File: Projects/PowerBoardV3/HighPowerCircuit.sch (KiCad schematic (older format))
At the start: 0 parts

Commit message: Added High Power Schematic
Added power Transistors
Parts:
- added D?: D_Small_ALT, symbol D_Small_ALT
- added J?: BATT, symbol Conn_01x02
- added Q? (x2): IRF3205, TO_SOT_Packages_THT:TO-220_Vertical, symbol IRF3205
- added Q?: BSS84, TO_SOT_Packages_SMD:SOT-23, symbol BSS84
- added R? (x2): 1M, symbol R_Small
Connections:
- new net: D?.1 (K), Q?.1 (G), R?.1, R?.2
- new net: D?.2 (A), Q?.3 (D), R?.1
- new net BATT+: J?.2 (Pin_2)
- new net BATT-: J?.1 (Pin_1), Q?.3 (S), R?.2
- new net CHG: Q?.2 (S)
- new net CHG_T: Q?.2 (D), Q?.2 (D)
- new net DSH: Q?.1 (G)
- new net GND: Q?.1 (G)
- new net SENSE_R: Q?.3 (S)
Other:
- note added: "High Power Circuit with Connectors\n"

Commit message: Changes to High Power Circuit
Added a bunch of changes that can be seen on the change log
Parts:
- added C? (x18): 680uF, symbol CP
- added J?: M3-ATX-20-PWR, symbol Conn_01x02
- added J?: Cell Voltage Sense, symbol Conn_02x04_Counter_Clockwise
- added J?: MC_STACK_1, symbol Conn_01x06
- added J?: MC_STACK_2, symbol Conn_01x06
- added J?: EXT_PWR_BLK_01, symbol Conn_01x18
- added J?: EXT_PWR_BLK_02, symbol Conn_01x18
- added J?: 12V_INT_PWR_BLK, symbol Conn_01x06
- added J?: 5V_INT_PWR_BLK, symbol Conn_01x06
- added J?: 3.3V_INT_PWR_BLK, symbol Conn_01x06
- added J?: 24V_INT_PWR_BLK, symbol Conn_01x06
- added P?: M3-ATX-20-PWRSUPP, symbol ATX-20-RESCUE-PowerBoardV2
- J?: value BATT -> BATT_PWR
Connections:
- net BATT+: now also C?.1, C?.1, C?.1, C?.1, C?.1, C?.1, J?.1 (Pin_1), J?.1 (Pin_1), J?.3 (Pin_3), J?.5 (Pin_5)
- net BATT-: now also C?.2, C?.2, C?.2, C?.2, C?.2, C?.2, J?.2 (Pin_2), J?.2 (Pin_2), J?.4 (Pin_4), J?.6 (Pin_6)
- new net: P?.10 (GND), P?.12 (GND), P?.14 (GND)
- new net +12V: J?.1 (Pin_1), J?.17 (Pin_17), J?.17 (Pin_17), J?.3 (Pin_3), J?.5 (Pin_5), P?.19 (+12v)
- new net +3.3V_1: J?.1 (Pin_1), J?.1 (Pin_1), J?.1 (Pin_1), P?.1 (+3v3)
- new net +3.3V_2: J?.3 (Pin_3), J?.3 (Pin_3), J?.3 (Pin_3), P?.2 (+3v3)
- new net +3.3V_3: J?.5 (Pin_5), J?.5 (Pin_5), J?.5 (Pin_5), P?.3 (+3v3)
- new net +5VSB: J?.13 (Pin_13), J?.13 (Pin_13), P?.17 (5VSB)
- new net +5V_1: J?.1 (Pin_1), J?.7 (Pin_7), J?.7 (Pin_7), P?.7 (+5v0)
- new net +5V_2: J?.3 (Pin_3), J?.9 (Pin_9), J?.9 (Pin_9), P?.11 (+5v0)
- new net +5V_3: J?.11 (Pin_11), J?.11 (Pin_11), J?.5 (Pin_5), P?.20 (+5v)
- new net +5v0: J?.15 (Pin_15), J?.15 (Pin_15), P?.18 (+5v0)
- new net -12V: J?.18 (Pin_18), J?.18 (Pin_18), J?.2 (Pin_2), J?.4 (Pin_4), J?.6 (Pin_6), P?.4 (-12v)
- new net -3.3V: J?.2 (Pin_2), J?.2 (Pin_2), J?.2 (Pin_2), J?.4 (Pin_4), J?.4 (Pin_4), J?.4 (Pin_4), J?.6 (Pin_6), J?.6 (Pin_6), J?.6 (Pin_6), P?.5 (GND)
- new net -5V: J?.10 (Pin_10), J?.10 (Pin_10), J?.12 (Pin_12), J?.12 (Pin_12), J?.14 (Pin_14), J?.14 (Pin_14), J?.16 (Pin_16), J?.16 (Pin_16), J?.2 (Pin_2), J?.4 (Pin_4), J?.6 (Pin_6), J?.8 (Pin_8), J?.8 (Pin_8), P?.16 (-5v)
- new net -5VSB: P?.9 (GND)
- new net -5v0: P?.6 (GND)
- new net CELL_1+: J?.1 (Pin_1)
- new net CELL_2+: J?.2 (Pin_2)
- new net CELL_3+: J?.3 (Pin_3)
- new net CELL_4+: J?.4 (Pin_4)
- new net CELL_5+: J?.5 (Pin_5)
- new net CELL_6+: J?.6 (Pin_6)
- new net CELL_7+: J?.7 (Pin_7)
- new net CELL_8+: J?.8 (Pin_8)
- new net MC1+: C?.1, J?.1 (Pin_1)
- new net MC1-: C?.2, J?.2 (Pin_2)
- new net MC2+: C?.1, J?.3 (Pin_3)
- new net MC2-: C?.2, J?.4 (Pin_4)
- new net MC3+: C?.1, J?.5 (Pin_5)
- new net MC3-: C?.2, J?.6 (Pin_6)
- new net MC4+: C?.1, J?.1 (Pin_1)
- new net MC4-: C?.2, J?.2 (Pin_2)
- new net MC5+: C?.1, J?.3 (Pin_3)
- new net MC5-: C?.2, J?.4 (Pin_4)
- new net MC6+: C?.1, J?.5 (Pin_5)
- new net MC6-: C?.2, J?.6 (Pin_6)
- new net PG: P?.15 (PG)
- new net P_OK: P?.8 (P_OK)
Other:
- note added: "Are these caps in series \nor parallel?\n"
- note added: "Battery Inputs"
- note added: "Cell Voltages are measured by \nIC in Low Power Schematic"
- note added: "Connector to be \nrated for 60A"
- note added: "Connectors are to be terminal blocks \nfor hardwire connection to motor controllers"
- note added: "External Power Terminal Block 1"
- note added: "External Power Terminal Block 2"
- note added: "Incoming PWR \nfrom Battery\n"
- note added: "Input for the PWRSUPP\n"
- note added: "Internal Power\nBlock 1"
- note added: "Internal Power\nBlock 2\n"
- note added: "Internal Power\nBlock 3\n"
- note added: "Internal Power\nBlock 4"
- note added: "Is this amount of capacitors \nwith these sizes really \nappropriate?"
- note added: "Located on Low \nPower Schematic"
- note added: "Main Power Supply for Voltages Less than 24V.\nGND here DOES NOT connect to BATT- so no GND symbol\nThe GND symbol that is used everywhere connects to BATT-"
- note added: "Motor Controller Terminal Blocks"
- note added: "Outgoing Power to \nMC_STACK_1\n"
- note added: "Outgoing Power to \nMC_STACK_2\n\n"
- note added: "Power Supply\n"
- note added: "Power Transistor Circuit"
- moved on the sheet: D?, J?, Q?, R?

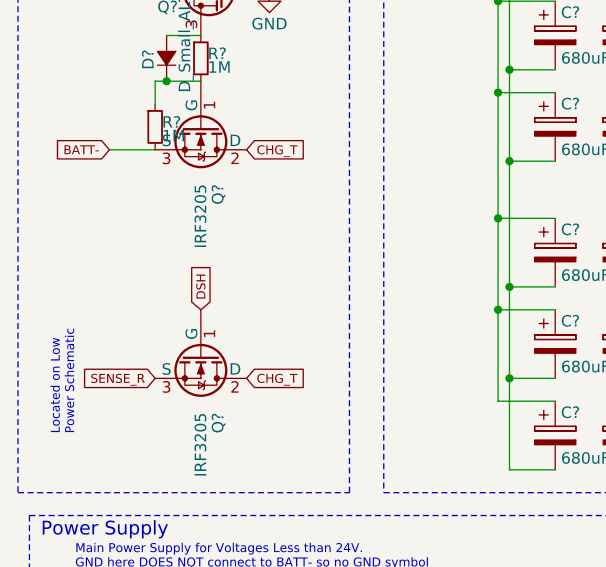
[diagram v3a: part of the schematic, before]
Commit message: Changed DSH to DSG and added initials to logs
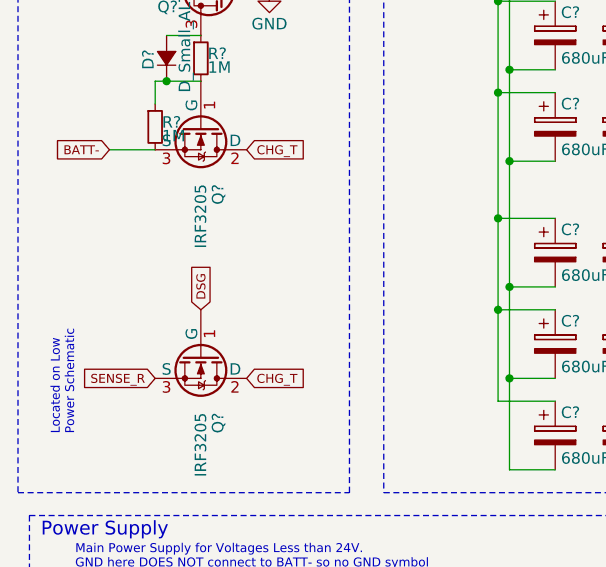
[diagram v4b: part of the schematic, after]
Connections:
- net DSH renamed DSG
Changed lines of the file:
@@
 $EndComp
 Text GLabel 1350 4250 1    39   Input ~ 0
-DSH
+DSG
 Text GLabel 1350 2650 1    39   Input ~ 0
 CHG

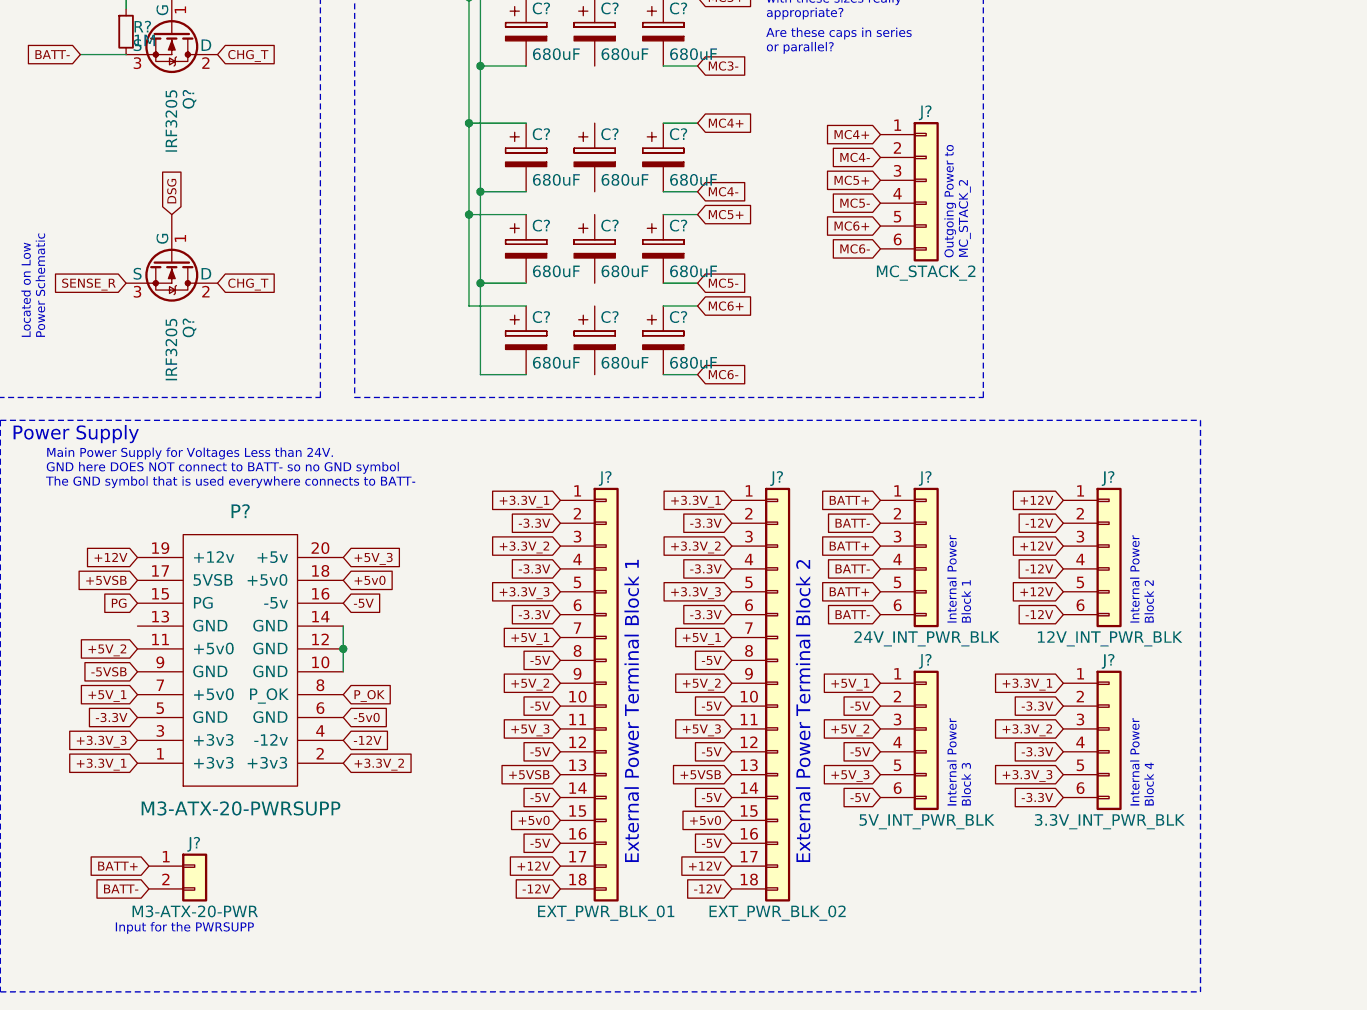
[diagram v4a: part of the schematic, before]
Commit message: Added Radio Barrel Jacks
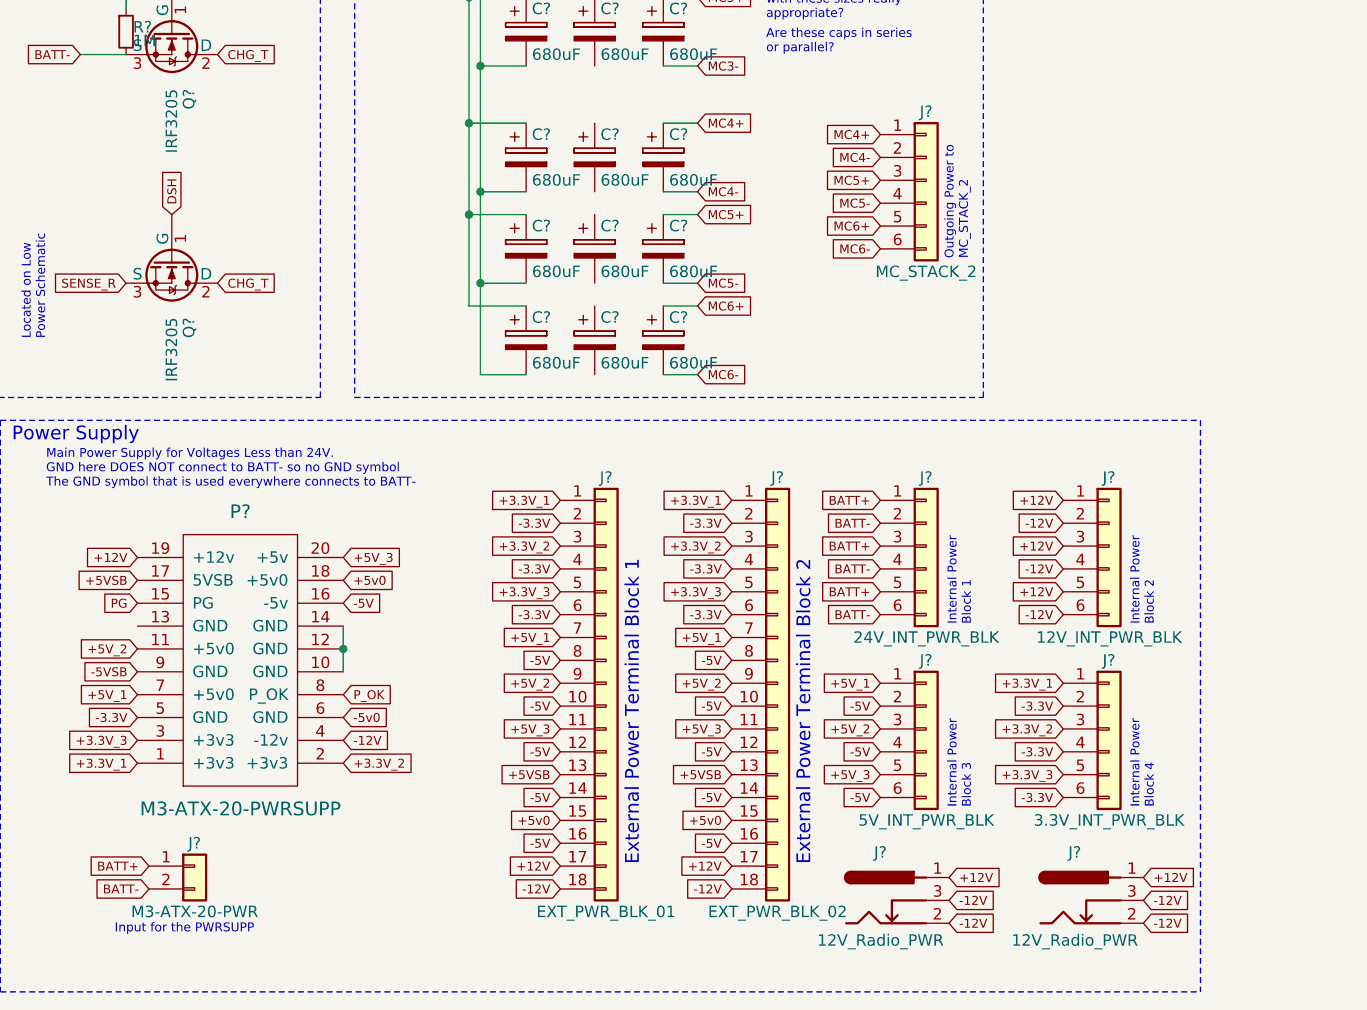
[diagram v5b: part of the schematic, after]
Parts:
- added J? (x2): 12V_Radio_PWR, symbol Barrel_Jack
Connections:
- net +12V: now also J?.1, J?.1
- net -12V: now also J?.2, J?.2, J?.3, J?.3
- net DSG renamed DSH
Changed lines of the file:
@@
 LIBS:power
 LIBS:device
-LIBS:switches
-LIBS:relays
-LIBS:motors
 LIBS:transistors
 LIBS:conn
@@
 LIBS:valves
 LIBS:USST-parts
-LIBS:dk_Addressable-Specialty
-LIBS:dk_Alarms-Buzzers-and-Sirens
-LIBS:dk_Automotive-Relays
-LIBS:dk_Balun
-LIBS:dk_Barrel-Audio-Connectors
-LIBS:dk_Battery-Holders-Clips-Contacts
-LIBS:dk_Clock-Timing-Clock-Generators-PLLs-Frequency-Synthesizers
-LIBS:dk_Clock-Timing-Programmable-Timers-and-Oscillators
-LIBS:dk_Clock-Timing-Real-Time-Clocks
-LIBS:dk_Coaxial-Connectors-RF
-LIBS:dk_Current-Transducers
-LIBS:dk_Data-Acquisition-ADCs-DACs-Special-Purpose
-LIBS:dk_Data-Acquisition-Analog-to-Digital-Converters-ADC
-LIBS:dk_Data-Acquisition-Digital-Potentiometers
-LIBS:dk_Data-Acquisition-Digital-to-Analog-Converters-DAC
-LIBS:dk_Data-Acquisition-Touch-Screen-Controllers
-LIBS:dk_DC-DC-Converters
-LIBS:dk_Digital-Isolators
-LIBS:dk_Diodes-Bridge-Rectifiers
-LIBS:dk_Diodes-Rectifiers-Arrays
-LIBS:dk_Diodes-Rectifiers-Single
-LIBS:dk_Diodes-Zener-Single
-LIBS:dk_Display-Modules-LED-Character-and-Numeric
-LIBS:dk_D-Sub-Connectors
-LIBS:dk_Embedded-Microcontrollers
-LIBS:dk_Encoders
-LIBS:dk_Evaluation-Boards-Sensors
-LIBS:dk_Ferrite-Beads-and-Chips
-LIBS:dk_Fixed-Inductors
-LIBS:dk_Fuses
-LIBS:dk_Gas-Sensors
-LIBS:dk_Humidity-Moisture-Sensors
-LIBS:dk_Image-Sensors-Camera
-LIBS:dk_Infrared-UV-Visible-Emitters
-LIBS:dk_Inrush-Current-Limiters-ICL
-LIBS:dk_Interface-Analog-Switches-Multiplexers-Demultiplexers
-LIBS:dk_Interface-Analog-Switches-Special-Purpose
-LIBS:dk_Interface-Controllers
-LIBS:dk_Interface-Drivers-Receivers-Transceivers
-LIBS:dk_Interface-I-O-Expanders
-LIBS:dk_Interface-Modules
-LIBS:dk_Interface-Sensor-and-Detector-Interfaces
-LIBS:dk_Interface-Sensor-Capacitive-Touch
-LIBS:dk_Interface-Specialized
-LIBS:dk_LED-Indication-Discrete
-LIBS:dk_LEDs-Circuit-Board-Indicators-Arrays-Light-Bars-Bar-Graphs
-LIBS:dk_Linear-Amplifiers-Audio
-LIBS:dk_Linear-Amplifiers-Instrumentation-OP-Amps-Buffer-Amps
-LIBS:dk_Linear-Comparators
-LIBS:dk_Logic-Buffers-Drivers-Receivers-Transceivers
-LIBS:dk_Logic-Flip-Flops
-LIBS:dk_Logic-Gates-and-Inverters
-LIBS:dk_Logic-Multivibrators
-LIBS:dk_Logic-Shift-Registers
-LIBS:dk_Logic-Signal-Switches-Multiplexers-Decoders
-LIBS:dk_Logic-Translators-Level-Shifters
-LIBS:dk_Magnetic-Sensors-Compass-Magnetic-Field-Modules
-LIBS:dk_Magnetic-Sensors-Linear-Compass-ICs
-LIBS:dk_Magnetic-Sensors-Switches-Solid-State
-LIBS:dk_Memory
-LIBS:dk_Memory-Connectors-PC-Card-Sockets
-LIBS:dk_Microphones
-LIBS:dk_Modular-Connectors-Jacks
-LIBS:dk_Modular-Connectors-Jacks-With-Magnetics
-LIBS:dk_Motion-Sensors-Accelerometers
-LIBS:dk_Motion-Sensors-IMUs-Inertial-Measurement-Units
-LIBS:dk_Motion-Sensors-Tilt-Switches
-LIBS:dk_Navigation-Switches-Joystick
-LIBS:dk_Optical-Sensors-Ambient-Light-IR-UV-Sensors
-LIBS:dk_Optical-Sensors-Photo-Detectors-Remote-Receiver
-LIBS:dk_Optical-Sensors-Photodiodes
-LIBS:dk_Optical-Sensors-Phototransistors
-LIBS:dk_Optical-Sensors-Reflective-Analog-Output
-LIBS:dk_Optoisolators-Logic-Output
-LIBS:dk_Optoisolators-Transistor-Photovoltaic-Output
-LIBS:dk_Optoisolators-Triac-SCR-Output
-LIBS:dk_Oscillators
-LIBS:dk_PMIC-AC-DC-Converters-Offline-Switchers
-LIBS:dk_PMIC-Battery-Chargers
-LIBS:dk_PMIC-Battery-Management
-LIBS:dk_PMIC-Current-Regulation-Management
-LIBS:dk_PMIC-Full-Half-Bridge-Drivers
-LIBS:dk_PMIC-Gate-Drivers
-LIBS:dk_PMIC-LED-Drivers
-LIBS:dk_PMIC-Motor-Drivers-Controllers
-LIBS:dk_PMIC-OR-Controllers-Ideal-Diodes
-LIBS:dk_PMIC-Power-Distribution-Switches-Load-Drivers
-LIBS:dk_PMIC-Power-Management-Specialized
-LIBS:dk_PMIC-RMS-to-DC-Converters
-LIBS:dk_PMIC-Supervisors
-LIBS:dk_PMIC-Thermal-Management
-LIBS:dk_PMIC-V-F-and-F-V-Converters
-LIBS:dk_PMIC-Voltage-Reference
-LIBS:dk_PMIC-Voltage-Regulators-DC-DC-Switching-Controllers
-LIBS:dk_PMIC-Voltage-Regulators-DC-DC-Switching-Regulators
-LIBS:dk_PMIC-Voltage-Regulators-Linear
-LIBS:dk_PMIC-Voltage-Regulators-Special-Purpose
-LIBS:dk_Power-Relays-Over-2-Amps
-LIBS:dk_Pressure-Sensors-Transducers
-LIBS:dk_Programmable-Oscillators
-LIBS:dk_Pushbutton-Switches
-LIBS:dk_Rectangular-Connectors-Headers-Male-Pins
-LIBS:dk_Reed-Relays
-LIBS:dk_Resistor-Networks-Arrays
-LIBS:dk_RF-Amplifiers
-LIBS:dk_RF-Antennas
-LIBS:dk_RF-Demodulators
-LIBS:dk_RF-Detectors
-LIBS:dk_RF-Evaluation-and-Development-Kits-Boards
-LIBS:dk_RFID-RF-Access-Monitoring-ICs
-LIBS:dk_RF-Receivers
-LIBS:dk_RF-Switches
-LIBS:dk_RF-Transceiver-ICs
-LIBS:dk_RF-Transceiver-Modules
-LIBS:dk_RF-Transmitters
-LIBS:dk_Rotary-Potentiometers-Rheostats
-LIBS:dk_Sensors-Transducers_Accessories
-LIBS:dk_Signal-Relays-Up-to-2-Amps
-LIBS:dk_Slide-Switches
-LIBS:dk_Solid-State-Relays
-LIBS:dk_Specialized-ICs
-LIBS:dk_Specialized-Sensors
-LIBS:dk_Surge-Suppression-ICs
-LIBS:dk_Tactile-Switches
-LIBS:dk_Temperature-Sensors-Analog-and-Digital-Output
-LIBS:dk_Thermal-Cutoffs-Thermal-Fuses
-LIBS:dk_Thyristors-DIACs-SIDACs
-LIBS:dk_Thyristors-SCRs
-LIBS:dk_Thyristors-TRIACs
-LIBS:dk_Toggle-Switches
-LIBS:dk_Transistors-Bipolar-BJT-Arrays
-LIBS:dk_Transistors-Bipolar-BJT-RF
-LIBS:dk_Transistors-Bipolar-BJT-Single
-LIBS:dk_Transistors-Bipolar-BJT-Single-Pre-Biased
-LIBS:dk_Transistors-FETs-MOSFETs-Arrays
-LIBS:dk_Transistors-FETs-MOSFETs-RF
-LIBS:dk_Transistors-FETs-MOSFETs-Single
-LIBS:dk_Transistors-JFETs
-LIBS:dk_Trimmer-Potentiometers
-LIBS:dk_TVS-Diodes
-LIBS:dk_TVS-Mixed-Technology
-LIBS:dk_USB-DVI-HDMI-Connectors
-LIBS:PowerBoardV3-cache
+LIBS:HighPowerCircuit-cache
 EELAYER 25 0
 EELAYER END
 $Descr A4 11693 8268
 encoding utf-8
-Sheet 2 3
+Sheet 1 1
 Title ""
 Date ""
@@
 $EndComp
 Text GLabel 1350 4250 1    39   Input ~ 0
-DSG
+DSH
 Text GLabel 1350 2650 1    39   Input ~ 0
 CHG
@@
 Text GLabel 4450 6000 0    39   Input ~ 0
 BATT-
+$Comp
+L Barrel_Jack J?
+U 1 1 5AA337D0
+P 4450 7250
+F 0 "J?" H 4450 7460 50  0000 C CNN
+F 1 "12V_Radio_PWR" H 4450 7075 50  0000 C CNN
+F 2 "" H 4500 7210 50  0001 C CNN
+F 3 "" H 4500 7210 50  0001 C CNN
+	1    4450 7250
+	1    0    0    -1
+$EndComp
+$Comp
+L Barrel_Jack J?
+U 1 1 5AA33946
+P 5300 7250
+F 0 "J?" H 5300 7460 50  0000 C CNN
+F 1 "12V_Radio_PWR" H 5300 7075 50  0000 C CNN
+F 2 "" H 5350 7210 50  0001 C CNN
+F 3 "" H 5350 7210 50  0001 C CNN
+	1    5300 7250
+	1    0    0    -1
+$EndComp
+Text GLabel 4750 7150 2    39   Input ~ 0
++12V
+Text GLabel 5600 7150 2    39   Input ~ 0
++12V
+Text GLabel 5600 7250 2    39   Input ~ 0
+-12V
+Text GLabel 5600 7350 2    39   Input ~ 0
+-12V
+Text GLabel 4750 7250 2    39   Input ~ 0
+-12V
+Text GLabel 4750 7350 2    39   Input ~ 0
+-12V
 $EndSCHEMATC

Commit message: Random
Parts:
- removed J?: EXT_PWR_BLK_01, symbol Conn_01x18
- removed J?: EXT_PWR_BLK_02, symbol Conn_01x18
- added J?: EXT_PWR_BLK_01, symbol Conn_01x20
- added J?: EXT_PWR_BLK_02, symbol Conn_01x20
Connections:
- net +12V: now also J?.17 (Pin_17), J?.17 (Pin_17)
- net +3.3V_1: now also J?.1 (Pin_1), J?.1 (Pin_1)
- net +3.3V_2: now also J?.3 (Pin_3), J?.3 (Pin_3)
- net +3.3V_3: now also J?.5 (Pin_5), J?.5 (Pin_5)
- net +5VSB: now also J?.13 (Pin_13), J?.13 (Pin_13)
- net +5V_1: now also J?.7 (Pin_7), J?.7 (Pin_7)
- net +5V_2: now also J?.9 (Pin_9), J?.9 (Pin_9)
- net +5V_3: now also J?.11 (Pin_11), J?.11 (Pin_11)
- net +5v0: now also J?.15 (Pin_15), J?.15 (Pin_15)
- net -12V: now also J?.18 (Pin_18), J?.18 (Pin_18)
- net -3.3V: now also J?.2 (Pin_2), J?.2 (Pin_2), J?.4 (Pin_4), J?.4 (Pin_4), J?.6 (Pin_6), J?.6 (Pin_6)
- net -5V: now also J?.10 (Pin_10), J?.10 (Pin_10), J?.12 (Pin_12), J?.12 (Pin_12), J?.14 (Pin_14), J?.14 (Pin_14), J?.16 (Pin_16), J?.16 (Pin_16), J?.8 (Pin_8), J?.8 (Pin_8)
- net BATT+: now also J?.19 (Pin_19), J?.19 (Pin_19)
- net BATT-: now also J?.20 (Pin_20), J?.20 (Pin_20)
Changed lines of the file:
@@
 	1350 3050 1200 3050
 Wire Wire Line
-	1150 3250 1350 3250
+	1150 3250 1200 3250
+Wire Wire Line
+	1200 3250 1350 3250
 $Comp
 L R_Small R?
@@
 Battery Inputs
 Wire Wire Line
-	2100 6050 2100 6250
+	2100 6050 2100 6150
+Wire Wire Line
+	2100 6150 2100 6250
 Connection ~ 2100 6150
 Text GLabel 3050 5500 0    39   Input ~ 0
@@
 MC3-
 Wire Wire Line
-	2600 2800 2900 2800
+	2600 2800 2700 2800
+Wire Wire Line
+	2700 2800 2900 2800
 Wire Wire Line
 	2900 3200 2700 3200
@@
 	2700 3600 2900 3600
 Wire Wire Line
-	2700 2800 2700 4950
+	2700 2800 2700 3200
+Wire Wire Line
+	2700 3200 2700 3600
+Wire Wire Line
+	2700 3600 2700 4150
+Wire Wire Line
+	2700 4150 2700 4550
+Wire Wire Line
+	2700 4550 2700 4950
 Connection ~ 2700 3200
 Wire Wire Line
 	2900 2900 2650 2900
 Wire Wire Line
-	2600 2500 2900 2500
+	2600 2500 2650 2500
+Wire Wire Line
+	2650 2500 2900 2500
 Wire Wire Line
 	2650 3300 2900 3300
 Wire Wire Line
-	2650 2500 2650 4650
+	2650 2500 2650 2900
+Wire Wire Line
+	2650 2900 2650 3300
+Wire Wire Line
+	2650 3300 2650 3850
+Wire Wire Line
+	2650 3850 2650 4250
+Wire Wire Line
+	2650 4250 2650 4650
 Connection ~ 2650 2900
 Connection ~ 2700 2800
@@
 Text GLabel 3800 7000 0    39   Input ~ 0
 -5V
-$Comp
-L Conn_01x18 J?
-U 1 1 5AA27119
-P 3250 6300
-F 0 "J?" H 3250 7200 50  0000 C CNN
-F 1 "EXT_PWR_BLK_01" H 3250 5300 50  0000 C CNN
-F 2 "" H 3250 6300 50  0001 C CNN
-F 3 "" H 3250 6300 50  0001 C CNN
-	1    3250 6300
-	1    0    0    -1
-$EndComp
-$Comp
-L Conn_01x18 J?
-U 1 1 5AA272EA
-P 4000 6300
-F 0 "J?" H 4000 7200 50  0000 C CNN
-F 1 "EXT_PWR_BLK_02" H 4000 5300 50  0000 C CNN
-F 2 "" H 4000 6300 50  0001 C CNN
-F 3 "" H 4000 6300 50  0001 C CNN
-	1    4000 6300
-	1    0    0    -1
-$EndComp
 Text Notes 1100 7400 0    39   ~ 0
 Input for the PWRSUPP\n
@@
 Text GLabel 4750 7350 2    39   Input ~ 0
 -12V
+$Comp
+L Conn_01x20 J?
+U 1 1 5AA34AB5
+P 3250 6400
+F 0 "J?" H 3250 7400 50  0000 C CNN
+F 1 "EXT_PWR_BLK_01" H 3250 5300 50  0000 C CNN
+F 2 "" H 3250 6400 50  0001 C CNN
+F 3 "" H 3250 6400 50  0001 C CNN
+	1    3250 6400
+	1    0    0    -1
+$EndComp
+Text GLabel 3050 7300 0    39   Input ~ 0
+BATT+
+Text GLabel 3050 7400 0    39   Input ~ 0
+BATT-
+$Comp
+L Conn_01x20 J?
+U 1 1 5AA34D97
+P 4000 6400
+F 0 "J?" H 4000 7400 50  0000 C CNN
+F 1 "EXT_PWR_BLK_02" H 4000 5300 50  0000 C CNN
+F 2 "" H 4000 6400 50  0001 C CNN
+F 3 "" H 4000 6400 50  0001 C CNN
+	1    4000 6400
+	1    0    0    -1
+$EndComp
+Text GLabel 3800 7300 0    39   Input ~ 0
+BATT+
+Text GLabel 3800 7400 0    39   Input ~ 0
+BATT-
 $EndSCHEMATC
